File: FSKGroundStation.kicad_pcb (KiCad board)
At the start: 4 copper layers, 100 x 82 mm, 177 parts, among them J1 FTSH-105-01-L-DV-K, J10 CX90B1-24P, J11 HTSW-102-07-G-S, J2 HTSW-102-07-G-S, J22 BWSMA-KWE-Z001, J24 HTSW-103-07-G-S, J3 CX90B1-24P, J4 BWSMA-KWE-Z001, J5 BWSMA-KWE-Z001, J9 HTSW-102-07-G-S, U1 TPSM861253RDXR, U10 74LVC1GU04DRL, U2 CC1312R1F3RGZR, U3 CY7C65215-32LTXI, U4 CC1125RHBR, U5 GRF5604, U6 SKYA21003, U7 GRF5604, U8 TPD4E004DRYR, U9 SKYA21003, Y1 OW7EL89CENUYO3YLC-40M, Y2 OW7EL89CANUXK7YLC-48M

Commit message: Add fiducials to the board
Signed-off-by: Corey Minyard <corey@minyard.net>
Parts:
- added FID1: Fiducial (round), Fiducial:Fiducial_1mm_Mask2mm, F.Cu at (72.4, 129.9)
- added FID10: Fiducial (square), footprints:Fiducial_Square_1mm_Mask2mm, B.Cu at (80.3, 134.7)
- added FID11: Fiducial (square), footprints:Fiducial_Square_1mm_Mask2mm, B.Cu at (80.5, 60.8)
- added FID12: Fiducial (square), footprints:Fiducial_Square_1mm_Mask2mm, B.Cu at (166.9, 129.0)
- added FID2: Fiducial (round), Fiducial:Fiducial_1mm_Mask2mm, F.Cu at (72.2, 68.4)
- added FID3: Fiducial (round), Fiducial:Fiducial_1mm_Mask2mm, F.Cu at (159.3, 136.2)
- added FID4: Fiducial (round), Fiducial:Fiducial_1mm_Mask2mm, B.Cu at (75.3, 129.5)
- added FID5: Fiducial (round), Fiducial:Fiducial_1mm_Mask2mm, B.Cu at (73.1, 67.8)
- added FID6: Fiducial (round), Fiducial:Fiducial_1mm_Mask2mm, B.Cu at (158.9, 135.9)
- added FID7: Fiducial (square), footprints:Fiducial_Square_1mm_Mask2mm, F.Cu at (80.7, 137.4)
- added FID8: Fiducial (square), footprints:Fiducial_Square_1mm_Mask2mm, F.Cu at (79.5, 60.0)
- added FID9: Fiducial (square), footprints:Fiducial_Square_1mm_Mask2mm, F.Cu at (166.9, 129.5)
- moved C48 1.57 mm to (141.6, 68.0)
- moved C47 1.42 mm to (142.9, 66.0)
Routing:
- net +5V: track 300.1 -> 295.8 mm
- net Net-(C81-Pad1): track 6.17 -> 5.15 mm

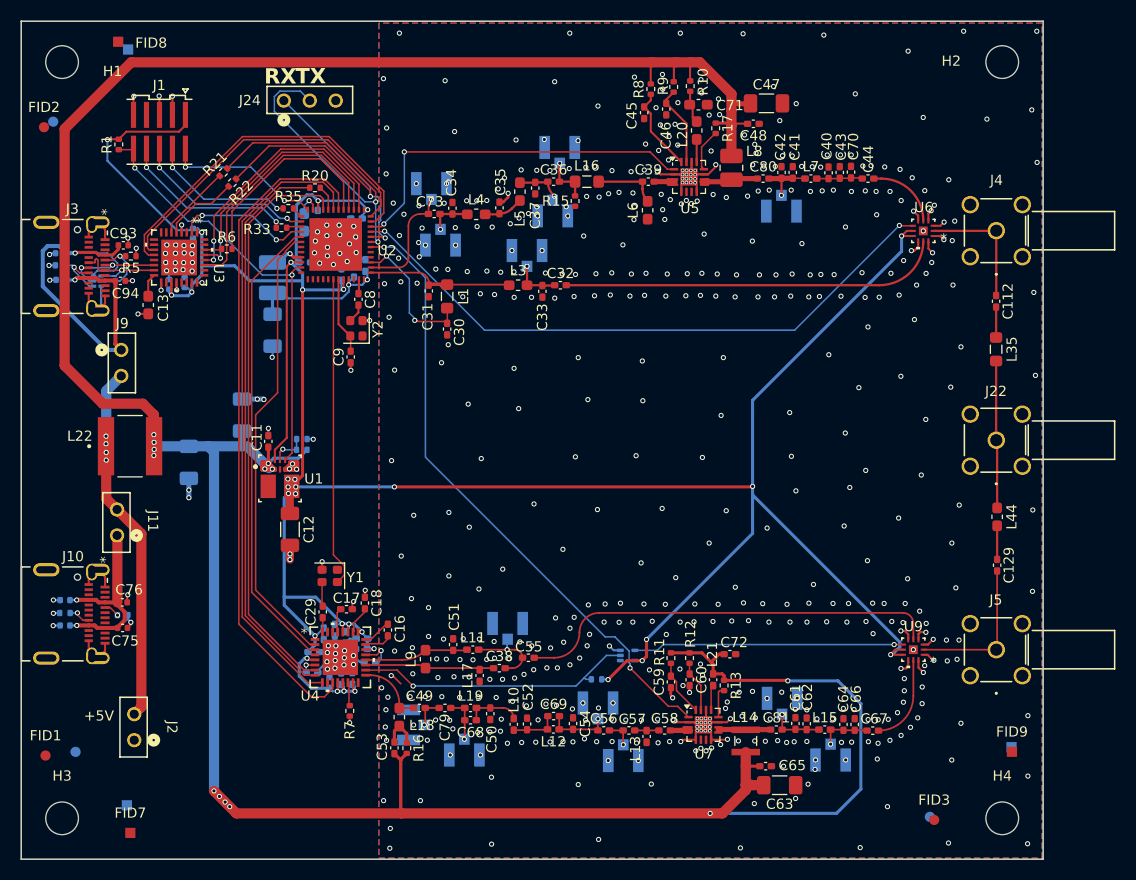
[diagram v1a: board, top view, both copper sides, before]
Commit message: Add fiduciaries and a control output
Signed-off-by: Corey Minyard <corey@minyard.net>
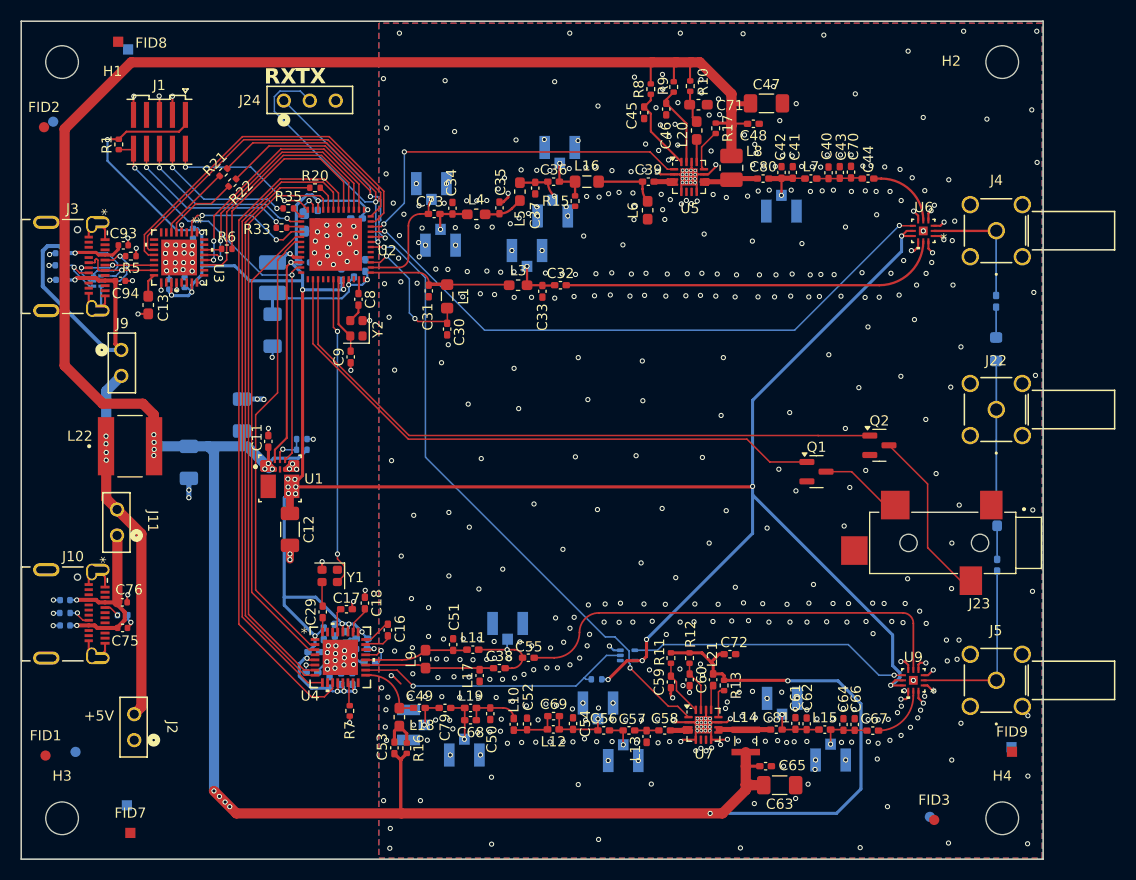
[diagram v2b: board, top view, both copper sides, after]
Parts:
- added J23: SJ-3524-SMT, footprints:CUI_SJ-3524-SMT, F.Cu at (163.8, 109.0)
- added Q1: BSS138, Package_TO_SOT_SMD:SOT-23, F.Cu at (147.8, 102.1)
- added Q2: BSS138, Package_TO_SOT_SMD:SOT-23, F.Cu at (154.0, 99.5)
- C112, C129, L35, L44: moved to B.Cu
- moved J22 3.00 mm to (165.4, 96.0)
- moved J5 3.00 mm to (165.4, 122.5)
- moved U9 3.00 mm to (157.3, 122.5)
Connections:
- U2 pad 38: unconnected-(U2-DIO_25-Pad38) -> TX_440_ON
- U2 pad 39: unconnected-(U2-DIO_26-Pad39) -> TX_144_ON
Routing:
- net TX_144_ON: track 0.00 -> 64.1 mm
- net TX_440_ON: track 0.00 -> 59.4 mm
- net Net-(Q2-D): track 0.00 -> 17.6 mm
- net Net-(Q1-D): track 0.00 -> 8.48 mm
- net +3.3V: track 298.3 -> 301.3 mm, vias 31 -> 30
- net /440MHz/440_TX: track 8.71 -> 5.71 mm
- net /440MHz/440_RX: track 41.5 -> 44.5 mm
- net RF_440: track 14.8 -> 17.8 mm
- net Net-(U9-CTRL): track 26.5 -> 27.7 mm
- net RADIO2_TCXO_POW: vias 0 -> 2
- net GND: vias 610 -> 606

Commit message: Add pull up on the PA enables
So they are off by default.

Signed-off-by: Corey Minyard <corey@minyard.net>
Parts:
- added R23: 10K, Resistor_SMD:R_0402_1005Metric, B.Cu at (107.0, 69.8)
- added R24: 10K, Resistor_SMD:R_0402_1005Metric, B.Cu at (106.9, 89.3)
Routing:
- net +3.3V: track 301.3 -> 332.4 mm, vias 30 -> 32
- net 440MHz_TX_ENABLE: track 61.3 -> 63.5 mm
- net 144MHz_TX_ENABLE: track 36.4 -> 37.4 mm

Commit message: Track cleanups
Signed-off-by: Corey Minyard <corey@minyard.net>
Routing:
- net +5V: track 295.8 -> 291.2 mm
- net GND: vias 606 -> 605

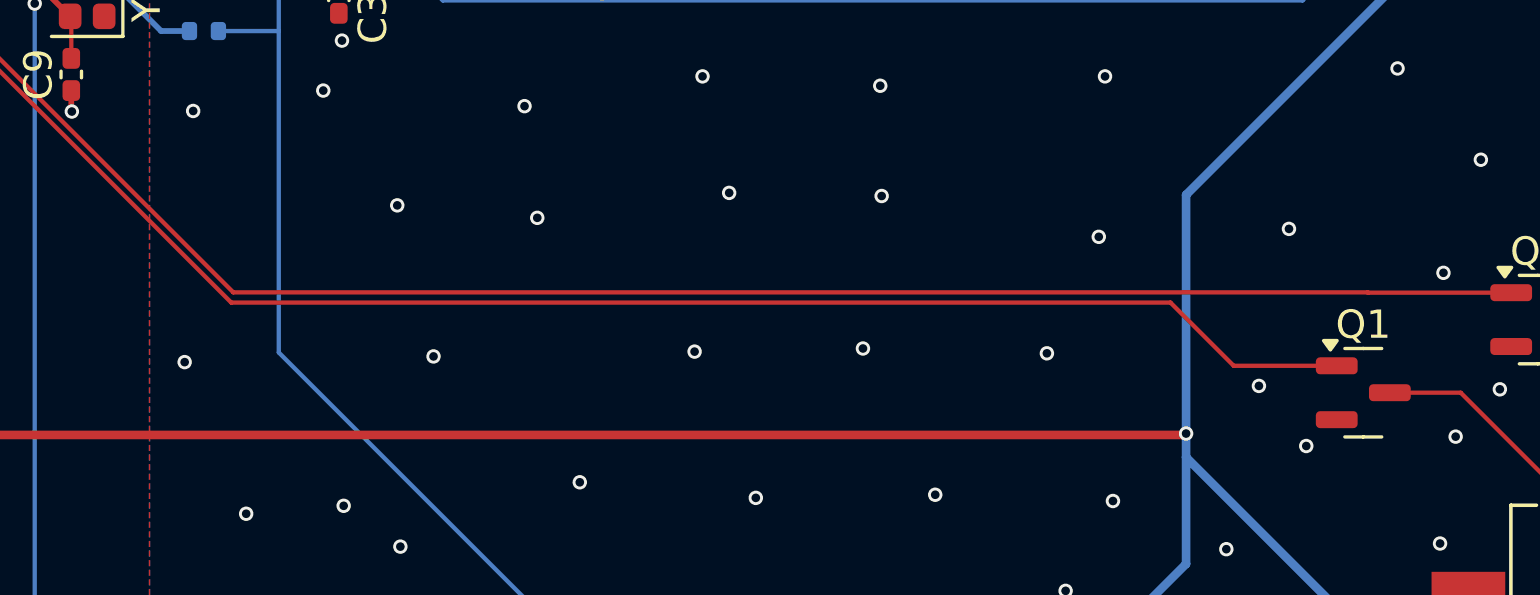
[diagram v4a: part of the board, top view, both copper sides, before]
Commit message: Add pulldowns on the external control transistor inputs
So they are disabled by default.

Signed-off-by: Corey Minyard <corey@minyard.net>
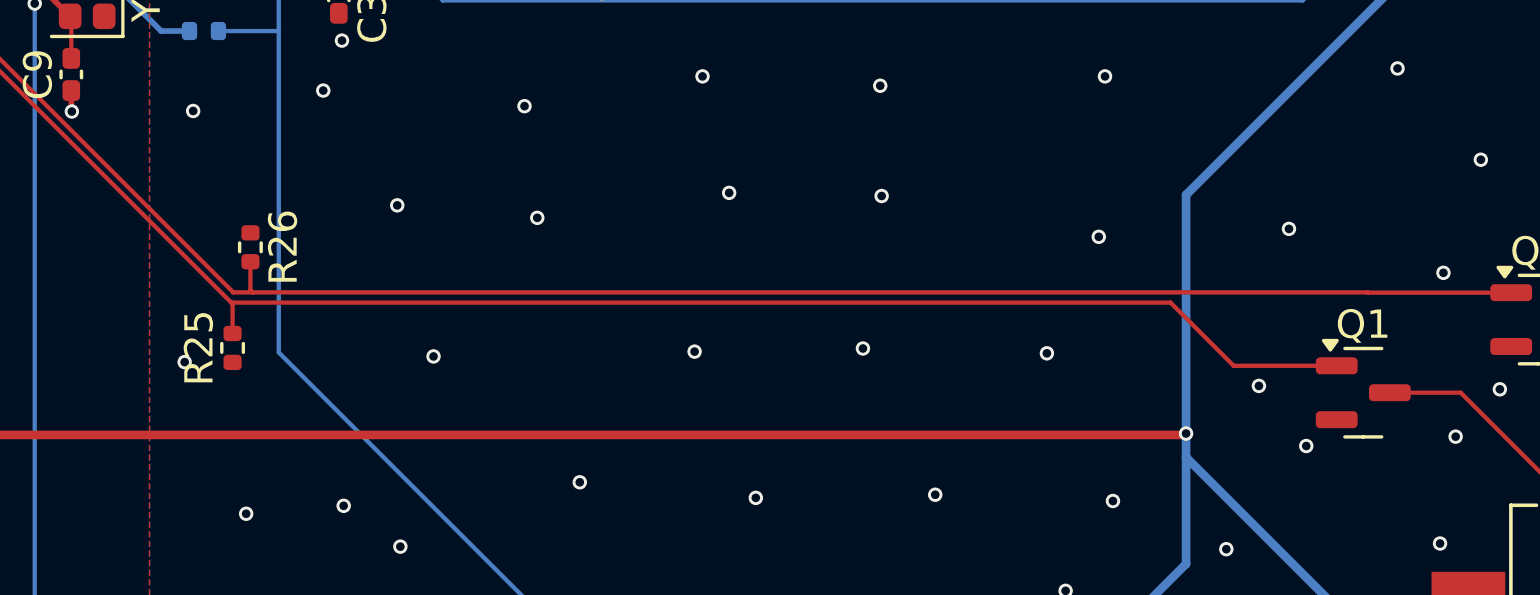
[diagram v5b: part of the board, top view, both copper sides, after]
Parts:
- added R25: 10K, Resistor_SMD:R_0402_1005Metric, F.Cu at (107.9, 100.5)
- added R26: 10K, Resistor_SMD:R_0402_1005Metric, F.Cu at (108.6, 97.0)
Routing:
- net TX_144_ON: track 64.1 -> 65.2 mm
- net TX_440_ON: track 59.4 -> 60.6 mm

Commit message: Change a resistor on the 150MHz TX
No need to have a 2K and a 1.96K resistor for this, just use 1.96K
on both.

Signed-off-by: Corey Minyard <corey@minyard.net>
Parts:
- R8: value 2K 1% -> 1.96K 1%
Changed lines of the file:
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@@
 			)
 		)
-		(property "Value" "2K 1%"
+		(property "Value" "1.96K 1%"
 			(at 0 1.17 90)
 			(layer "F.Fab")
